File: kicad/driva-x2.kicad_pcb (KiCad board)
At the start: 4 copper layers, 100 x 50 mm, 199 parts, among them J1 CONN_HALL_1, J10 CONN_SPI_2, J11 CONN_CAN, J12 CONN_POWER, J2 CONN_PROG, J3 CONN_USB_OTG, J4 CONN_I2C, J5 CONN_POWER2, J6 CONN_SERVO, J8 CONN_SPI_1, J9 CONN_HALL_2, Q1 TPH1R403NL, Q10 TPH1R403NL, Q11 TPH1R403NL, Q12 TPH1R403NL, Q2 TPH1R403NL, Q3 TPH1R403NL, Q4 TPH1R403NL, Q5 TPH1R403NL, Q6 TPH1R403NL, Q7 TPH1R403NL, Q8 TPH1R403NL, Q9 TPH1R403NL, SW1 push, SW2 push, SW3 push, U1 INA240A2PW, U10 L6387ED, U11 INA240A2PW, U12 L6387ED, U13 AMS1117-3.3, U14 TJA1051T-3, U15 STM32F405RGTx, U2 L6387ED, U3 INA240A2PW, U4 L6387ED, U5 INA240A2PW, U6 L6387ED, U7 INA240A2PW, U8 L6387ED, U9 INA240A2PW

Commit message: Adding 0.9 version
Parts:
- removed C62, C64, C66, C68: 100n, Capacitor_SMD:C_0402_1005Metric
- removed C63, C65, C67: 1n, Capacitor_SMD:C_0402_1005Metric
- removed D10: BLUE, LED_SMD:LED_0603_1608Metric
- removed D11, D6, D7: b5819w, Diode_SMD:D_SOD-123
- removed D8: RED, LED_SMD:LED_0603_1608Metric
- removed D9: GREEN, LED_SMD:LED_0603_1608Metric
- removed H10: PAD_W_2, Connector_Wire:SolderWire-2.5sqmm_1x01_D2.4mm_OD4.4mm
- removed H5: PAD_U_1, Connector_Wire:SolderWire-2.5sqmm_1x01_D2.4mm_OD4.4mm
- removed H6: PAD_V_1, Connector_Wire:SolderWire-2.5sqmm_1x01_D2.4mm_OD4.4mm
- removed H7: PAD_W_1, Connector_Wire:SolderWire-2.5sqmm_1x01_D2.4mm_OD4.4mm
- removed H8: PAD_U_2, Connector_Wire:SolderWire-2.5sqmm_1x01_D2.4mm_OD4.4mm
- removed H9: PAD_V_2, Connector_Wire:SolderWire-2.5sqmm_1x01_D2.4mm_OD4.4mm
- removed Q1, Q10, Q11, Q12, Q2, Q3, Q4, Q5, Q6, Q7, Q8, Q9: TPH1R403NL, Package_SO:SOP-8-1EP_4.57x4.57mm_P1.27mm_EP4.57x4.45mm_ThermalVias
- removed R53: 3K3, Resistor_SMD:R_0402_1005Metric
- removed R54: 4k7, Resistor_SMD:R_0402_1005Metric
- removed R55: 10k, Resistor_SMD:R_0402_1005Metric
- removed R56, R57, R58, R59, R60, R61, R62, R63, R64: 1K, Resistor_SMD:R_0402_1005Metric
- removed TH1, TH2: Thermistor, Resistor_SMD:R_0603_1608Metric
- removed U11: INA240A2PW, Package_SO:TSSOP-8_4.4x3mm_P0.65mm
- removed U12: L6387ED, Package_SO:SOIC-8_3.9x4.9mm_P1.27mm
- removed U13: AMS1117-3.3, Package_TO_SOT_SMD:SOT-223-3_TabPin2
- removed U14: TJA1051T-3, Package_SO:SOIC-8_3.9x4.9mm_P1.27mm
- removed U15: STM32F405RGTx, Package_QFP:LQFP-64_10x10mm_P0.5mm
- added J7: CONN_SPI_1, Connector_PinHeader_2.54mm:PinHeader_1x06_P2.54mm_Vertical, F.Cu at (64.3, 68.8)
- added L1: 2.2uh, Inductor_SMD:L_1210_3225Metric, F.Cu at (110.0, 57.5)
- C1: value 1u -> 10u
- C10, C20, C25, C30, C5, C53: value 10n -> 100n
- C11, C6: value 1u -> 100n; footprint Capacitor_SMD:C_0603_1608Metric -> Capacitor_SMD:C_0402_1005Metric
- C12: value 100p -> 10u
- C13: value 100p -> 4.7u+; footprint Capacitor_SMD:C_0402_1005Metric -> Capacitor_SMD:C_0805_2012Metric
- C14, C4, C9: value 470n -> 100n; footprint Capacitor_SMD:C_0603_1608Metric -> Capacitor_SMD:C_0402_1005Metric
- C16: value 1u -> 12p; footprint Capacitor_SMD:C_0603_1608Metric -> Capacitor_SMD:C_0402_1005Metric
- C17: value 100p -> 12p
- C18, C2, C3, C7, C8: value 100p -> 100n
- C19: value 470n -> 2.2u
- C21: value 1u -> 2.2u
- C22, C23: value 100p -> 2.2u; footprint Capacitor_SMD:C_0402_1005Metric -> Capacitor_SMD:C_0603_1608Metric
- C24: value 470n -> 10u
- C26: value 1u -> 220n+
- C27: value 100p -> 100n+; footprint Capacitor_SMD:C_0402_1005Metric -> Capacitor_SMD:C_0603_1608Metric
- C28: value 100p -> 220n+; footprint Capacitor_SMD:C_0402_1005Metric -> Capacitor_SMD:C_0603_1608Metric
- C29: value 470n -> 1n; footprint Capacitor_SMD:C_0603_1608Metric -> Capacitor_SMD:C_0402_1005Metric
- C31, C54: value 10u -> 220n+
- C32, C37: value 100n -> 100n+; footprint Capacitor_SMD:C_0402_1005Metric -> Capacitor_SMD:C_0603_1608Metric
- C33, C36, C38, C49, C56: value 100n -> 220n+; footprint Capacitor_SMD:C_0402_1005Metric -> Capacitor_SMD:C_0603_1608Metric
- C34, C39: value 100n -> 1n
- C41, C42: value 10u -> 100n; footprint Capacitor_SMD:C_0805_2012Metric -> Capacitor_SMD:C_0402_1005Metric
- C43: value 100n -> 2.2n
- C44: value 10n -> 220n+; footprint Capacitor_SMD:C_0402_1005Metric -> Capacitor_SMD:C_0603_1608Metric
- C45: value 12p -> 100n+; footprint Capacitor_SMD:C_0402_1005Metric -> Capacitor_SMD:C_0603_1608Metric
- C46: value 12p -> 220n+; footprint Capacitor_SMD:C_0402_1005Metric -> Capacitor_SMD:C_0603_1608Metric
- C47, C52: value 2.2u -> 1n; footprint Capacitor_SMD:C_0603_1608Metric -> Capacitor_SMD:C_0402_1005Metric
- C50: value 2.2u -> 100n+
- C51: value 2.2u -> 220n+
- C55: value 10n -> 100n+; footprint Capacitor_SMD:C_0402_1005Metric -> Capacitor_SMD:C_0603_1608Metric
- C59: value 1n -> 33p
- C60: value 100n -> 1000u+; footprint Capacitor_SMD:C_0402_1005Metric -> Capacitor_THT:CP_Radial_D8.0mm_P5.00mm
- C61: value 1n -> 10n
- D2: value b5819w -> RED; footprint Diode_SMD:D_SOD-123 -> LED_SMD:LED_0603_1608Metric
- D3: value b5819w -> GREEN; footprint Diode_SMD:D_SOD-123 -> LED_SMD:LED_0603_1608Metric
- D4: value b5819w -> BLUE; footprint Diode_SMD:D_SOD-123 -> LED_SMD:LED_0603_1608Metric
- H1, H2, H3, H4: footprint MountingHole:MountingHole_3.2mm_M3_Pad_Via -> MountingHole:MountingHole_3.2mm_M3_ISO14580_Pad_TopBottom
- J10: value CONN_SPI_2 -> CONN_CAN; footprint Connector_PinHeader_2.54mm:PinHeader_1x06_P2.54mm_Vertical -> Connector_PinHeader_2.54mm:PinHeader_1x04_P2.54mm_Vertical
- J11: value CONN_CAN -> CONN_PWR; footprint Connector_PinHeader_2.54mm:PinHeader_1x04_P2.54mm_Vertical -> TerminalBlock:TerminalBlock_Altech_AK300-2_P5.00mm
- J12: value CONN_POWER -> CONN_SERIAL; footprint Connector_AMASS:AMASS_XT60-M_1x02_P7.20mm_Vertical -> Connector_PinHeader_2.54mm:PinHeader_1x04_P2.54mm_Vertical
- J2: footprint Connector_PinHeader_2.54mm:PinHeader_1x05_P2.54mm_Vertical -> Connector_PinHeader_2.54mm:PinHeader_1x04_P2.54mm_Vertical
- J3: footprint Connector_USB:USB_Micro-B_GCT_USB3076-30-A -> Connector_USB:USB_Micro-B_Wuerth_629105150521
- J4: value CONN_I2C -> CONN_MOT_1; footprint Connector_PinHeader_2.54mm:PinHeader_1x04_P2.54mm_Vertical -> TerminalBlock:TerminalBlock_Altech_AK300-3_P5.00mm
- J5: value CONN_POWER2 -> CONN_SERIAL; footprint Connector_PinHeader_2.54mm:PinHeader_1x02_P2.54mm_Vertical -> Connector_PinHeader_2.54mm:PinHeader_1x04_P2.54mm_Vertical
- J6: value CONN_SERVO -> CONN_MOT_2; footprint Connector_PinHeader_2.54mm:PinHeader_1x05_P2.54mm_Vertical -> TerminalBlock:TerminalBlock_Altech_AK300-3_P5.00mm
- J8: value CONN_SPI_1 -> CONN_SPI_2
- R10: value 33 -> 220; footprint Resistor_SMD:R_0603_1608Metric -> Resistor_SMD:R_0402_1005Metric
- R11: value 10k -> 2K2; footprint Resistor_SMD:R_0402_1005Metric -> Resistor_SMD:R_0603_1608Metric
- R12, R30, R42: value 0.002R @1W -> 10k; footprint Resistor_SMD:R_1206_3216Metric -> Resistor_SMD:R_0402_1005Metric
- R13, R22, R25, R34, R37: value 33 -> 10k; footprint Resistor_SMD:R_0603_1608Metric -> Resistor_SMD:R_0402_1005Metric
- R14: value 1 -> 120R+; footprint Resistor_SMD:R_0603_1608Metric -> Resistor_SMD:R_1206_3216Metric
- R15: value 10k -> 33K
- R16: value 33 -> 3K3; footprint Resistor_SMD:R_0603_1608Metric -> Resistor_SMD:R_0402_1005Metric
- R18: value 0.002R @1W -> 1K; footprint Resistor_SMD:R_1206_3216Metric -> Resistor_SMD:R_0402_1005Metric
- R19: value 33 -> 1K; footprint Resistor_SMD:R_0603_1608Metric -> Resistor_SMD:R_0402_1005Metric
- R20: value 1 -> 1K; footprint Resistor_SMD:R_0603_1608Metric -> Resistor_SMD:R_0402_1005Metric
- R23, R27, R35, R39: value 10k -> 1k
- R24, R36: value 0.002R @1W -> 510R; footprint Resistor_SMD:R_1206_3216Metric -> Resistor_SMD:R_0402_1005Metric
- R26, R38: value 1 -> 10k; footprint Resistor_SMD:R_0603_1608Metric -> Resistor_SMD:R_0402_1005Metric
- R28, R40: value 33 -> 510R; footprint Resistor_SMD:R_0603_1608Metric -> Resistor_SMD:R_0402_1005Metric
- R31, R43: value 33 -> 1k; footprint Resistor_SMD:R_0603_1608Metric -> Resistor_SMD:R_0402_1005Metric
- R32, R44: value 1 -> 510R; footprint Resistor_SMD:R_0603_1608Metric -> Resistor_SMD:R_0402_1005Metric
- R45: value 10k -> 400K
- R46: value 220 -> 4.7k
- R47: value 2K2 -> 4.7k; footprint Resistor_SMD:R_0603_1608Metric -> Resistor_SMD:R_0402_1005Metric
- R48: value 10k -> 4.7k
- R49: value 10k -> 120k
- R50: value 220 -> 39k
- R51: value 33K -> 10k
- R52: value 4k7 -> 10k
- U1: value INA240A2PW -> mp2451dt; footprint Package_SO:TSSOP-8_4.4x3mm_P0.65mm -> Package_TO_SOT_SMD:SOT-23-6
- U10, U4, U6, U8: value L6387ED -> IFX007T; footprint Package_SO:SOIC-8_3.9x4.9mm_P1.27mm -> Package_TO_SOT_SMD:TO-263-7_TabPin8
- U2: value L6387ED -> TJA1051T-3
- U3: value INA240A2PW -> STM32F405RGTx; footprint Package_SO:TSSOP-8_4.4x3mm_P0.65mm -> Package_QFP:LQFP-64_10x10mm_P0.5mm
- U5, U9: value INA240A2PW -> IFX007T; footprint Package_SO:TSSOP-8_4.4x3mm_P0.65mm -> Package_TO_SOT_SMD:TO-263-7_TabPin8
- U7: value INA240A2PW -> MPU-6050; footprint Package_SO:TSSOP-8_4.4x3mm_P0.65mm -> Sensor_Motion:InvenSense_QFN-24_4x4mm_P0.5mm
- moved H1 102.6 mm to (65.6, 33.6)
- moved R14 101.6 mm to (74.5, 84.8), turned to 0 degrees
- moved H3 98.0 mm to (158.4, 86.5)
- moved J10 85.3 mm to (70.7, 87.8), turned to 90 degrees
- moved U2 84.6 mm to (74.7, 80.0), turned to 270 degrees
- moved U7 82.4 mm to (149.3, 80.3), turned to 90 degrees
- moved R13 79.2 mm to (91.5, 85.5)
- moved C58 77.8 mm to (92.5, 63.9)
- moved C57 77.6 mm to (92.5, 60.9), turned to 0 degrees
- moved R11 77.2 mm to (97.7, 87.8)
- moved C5 77.1 mm to (102.4, 81.0)
- moved R17 72.0 mm to (80.8, 85.0), turned to 90 degrees
- moved J4 71.0 mm to (66.4, 50.3)
- moved J6 70.1 mm to (157.6, 50.2)
- moved R18 62.6 mm to (101.3, 87.3), turned to 90 degrees
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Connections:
- C1 pad 1: Net-(C1-Pad1) -> GND
- C1 pad 2: Net-(C1-Pad2) -> +3V3
- C10 pad 1: Net-(C10-Pad1) -> GND
- C10 pad 2: GND -> +3V3
- C12 pad 1: /driver_2/HIN_W -> GND
- C12 pad 2: GND -> +3V3
- C13 pad 1: /driver_2/LIN_W -> GND
- C13 pad 2: GND -> Net-(C13-Pad2)
- C14 pad 1: VCC -> GND
- C14 pad 2: GND -> +3.3VA
- C15 pad 1: Net-(C15-Pad1) -> GND
- C15 pad 2: GND -> +3.3VA
- C16 pad 1: Net-(C16-Pad1) -> HSE_IN
- C16 pad 2: Net-(C16-Pad2) -> GND
- C17 pad 1: /driver_1/HIN_U -> Net-(C17-Pad1)
- C18 pad 1: /driver_1/LIN_U -> BOOT0
- C19 pad 1: VCC -> GND
- C19 pad 2: GND -> +3V3
- C2 pad 1: /driver_2/HIN_U -> GND
- C2 pad 2: GND -> +3V3
- C20 pad 1: Net-(C20-Pad1) -> NRST
- C21 pad 1: Net-(C21-Pad1) -> GND
- C21 pad 2: Net-(C21-Pad2) -> +3V3
- C22 pad 1: /driver_1/HIN_V -> Net-(C22-Pad1)
- C23 pad 1: /driver_1/LIN_V -> Net-(C23-Pad1)
- C24 pad 1: VCC -> GND
- C24 pad 2: GND -> BATTERY
- C25 pad 1: Net-(C25-Pad1) -> USER_BUTTON
- C26 pad 1: Net-(C26-Pad1) -> /driver-2/OUT_U
- C26 pad 2: Net-(C26-Pad2) -> VCC
- C27 pad 1: /driver_1/HIN_W -> VCC
- C28 pad 1: /driver_1/LIN_W -> VCC
- C29 pad 1: VCC -> /driver-2/SENSE_U
- C3 pad 1: /driver_2/LIN_U -> GND
- C3 pad 2: GND -> +3V3
- C31 pad 1: GND -> /driver-2/OUT_V
- C31 pad 2: +3V3 -> VCC
- C32 pad 1: GND -> VCC
- C32 pad 2: +3V3 -> GND
- C33 pad 1: GND -> VCC
- C33 pad 2: +3V3 -> GND
- C34 pad 1: GND -> /driver-2/SENSE_V
- C34 pad 2: +3V3 -> GND
- C35 pad 1: GND -> Net-(C35-Pad1)
- C35 pad 2: +3V3 -> GND
- C36 pad 1: GND -> /driver-2/OUT_W
- C36 pad 2: +3V3 -> VCC
- C37 pad 1: GND -> VCC
- C37 pad 2: +3V3 -> GND
- C38 pad 1: GND -> VCC
- C38 pad 2: +3V3 -> GND
- C39 pad 1: GND -> /driver-2/SENSE_W
- C39 pad 2: +3V3 -> GND
- C4 pad 1: VCC -> GND
- C4 pad 2: GND -> +3V3
- C40 pad 1: GND -> Net-(C40-Pad1)
- C40 pad 2: +3V3 -> GND
- C41 pad 2: Net-(C41-Pad2) -> +3V3
- C42 pad 2: +3V3 -> Net-(C42-Pad2)
- C43 pad 2: +3.3VA -> Net-(C43-Pad2)
- C44 pad 1: GND -> /driver-1/OUT_U
- C44 pad 2: +3.3VA -> VCC
- C45 pad 1: HSE_IN -> VCC
- C46 pad 1: Net-(C46-Pad1) -> VCC
- C47 pad 1: GND -> /driver-1/SENSE_U
- C47 pad 2: +3V3 -> GND
- C48 pad 1: BOOT0 -> Net-(C48-Pad1)
- C49 pad 1: NRST -> /driver-1/OUT_V
- C49 pad 2: GND -> VCC
- C5 pad 1: Net-(C5-Pad1) -> GND
- C5 pad 2: GND -> +3V3
- C50 pad 1: GND -> VCC
- C50 pad 2: +3V3 -> GND
- C51 pad 1: Net-(C51-Pad1) -> VCC
- C52 pad 1: Net-(C52-Pad1) -> /driver-1/SENSE_V
- C53 pad 1: TEMP_1 -> Net-(C53-Pad1)
- C54 pad 1: GND -> /driver-1/OUT_W
- C54 pad 2: BATTERY -> VCC
- C55 pad 1: TEMP_2 -> VCC
- C56 pad 1: USER_BUTTON -> VCC
- C57 pad 1: /driver_2/SENSE_U -> /driver-1/SENSE_W
- C58 pad 1: +3V3 -> Net-(C58-Pad1)
- C59 pad 1: /driver_2/SENSE_V -> Net-(C59-Pad1)
- C59 pad 2: GND -> +3V3
- C6 pad 1: Net-(C6-Pad1) -> GND
- C6 pad 2: Net-(C6-Pad2) -> +3V3
- C60 pad 1: +3V3 -> VCC
- C61 pad 1: /driver_2/SENSE_W -> +3V3
- C7 pad 1: /mcu/HIN_U_2 -> GND
- C7 pad 2: GND -> +3V3
- C8 pad 1: /mcu/LIN_U_2 -> GND
- C8 pad 2: GND -> +3V3
- C9 pad 1: VCC -> GND
- C9 pad 2: GND -> +3V3
- D1 pad 1: Net-(C1-Pad2) -> Net-(D1-Pad1)
- D2 pad 1: Net-(C6-Pad2) -> Net-(D2-Pad1)
- D2 pad 2: VCC -> +3V3
- D3 pad 1: Net-(C11-Pad2) -> Net-(D3-Pad1)
- D3 pad 2: VCC -> LED_GREEN
- D4 pad 1: Net-(C16-Pad2) -> Net-(D4-Pad1)
- D4 pad 2: VCC -> LED_BLUE
- D5 pad 1: Net-(C21-Pad2) -> Net-(C11-Pad1)
- D5 pad 2: VCC -> GND
- FB1 pad 1: Net-(C41-Pad2) -> Net-(C13-Pad2)
- FB1 pad 2: Net-(D11-Pad1) -> Net-(D1-Pad1)
- HSE1 pad 3: Net-(C46-Pad1) -> Net-(C17-Pad1)
- J1 pad 2: /mcu/HALL_U_1 -> /mcu/HALL_U1
- J1 pad 3: /mcu/HALL_V_1 -> /mcu/HALL_V1
- J1 pad 4: /mcu/HALL_W_1 -> /mcu/HALL_W1
- J10 pad 2: /mcu/SPI3_SS2 -> /mcu/CAN_L
- J10 pad 3: /mcu/SPI3_MISO -> /mcu/CAN_H
- J10 pad 4: /mcu/SPI3_MOSI -> +3V3
- J11 pad 2: /mcu/CAN_H -> VCC
- J12 pad 2: VCC -> /mcu/I2C1_SCL
- J2 pad 1: /mcu/JTAG_DO -> /mcu/SWO
- J2 pad 2: /mcu/JTAG_DI -> /mcu/SWCLK
- J2 pad 3: /mcu/SWCLK -> GND
- J2 pad 4: GND -> /mcu/SWDIO
- J4 pad 1: GND -> /driver-1/OUT_W
- J4 pad 2: /mcu/I2C_1_SCL -> /driver-1/OUT_V
- J4 pad 3: /mcu/I2C_1_SDA -> /driver-1/OUT_U
- J5 pad 1: Net-(J3-Pad1) -> GND
- J5 pad 2: ALT_POWER -> /mcu/USART1_TX
- J6 pad 1: GND -> /driver-2/OUT_W
- J6 pad 2: /mcu/USART1_TX -> /driver-2/OUT_V
- J6 pad 3: /mcu/USART1_RX -> /driver-2/OUT_U
- J8 pad 2: /mcu/SPI3_SS1 -> /mcu/SPI3_SS2
- J8 pad 3: /mcu/SPI3_MISO -> SPI3_MOSI
- J8 pad 4: /mcu/SPI3_MOSI -> SPI3_MISO
- J8 pad 5: /mcu/SPI3_SCLK -> SPI3_SCLK
- J9 pad 2: /mcu/HALL_U_I2C_2_SCL -> /mcu/HALL_U2
- J9 pad 3: /mcu/HALL_V_I2C_2_SDA -> /mcu/HALL_V2
- J9 pad 4: /mcu/HALL_W_2 -> /mcu/HALL_W2
- R10 pad 1: Net-(Q1-Pad4) -> HSE_OUT
- R10 pad 2: Net-(C1-Pad1) -> Net-(C17-Pad1)
- R11 pad 1: Net-(Q1-Pad1) -> NRST
- R11 pad 2: Net-(Q1-Pad4) -> +3V3
- R12 pad 1: /driver_2/OUT_U -> GND
- R12 pad 2: Net-(Q1-Pad1) -> BOOT1
- R13 pad 1: Net-(Q2-Pad4) -> GND
- R13 pad 2: Net-(R13-Pad2) -> BOOT0
- R14 pad 1: Net-(C5-Pad1) -> /mcu/CAN_L
- R14 pad 2: Net-(Q1-Pad1) -> /mcu/CAN_H
- R15 pad 1: GND -> BATTERY
- R15 pad 2: Net-(Q2-Pad4) -> VCC
- R16 pad 1: Net-(Q3-Pad4) -> GND
- R16 pad 2: Net-(C6-Pad1) -> BATTERY
- R17 pad 1: Net-(Q3-Pad1) -> USER_BUTTON
- R17 pad 2: Net-(Q3-Pad4) -> GND
- R18 pad 1: /driver_2/OUT_V -> GND
- R18 pad 2: Net-(Q3-Pad1) -> Net-(D2-Pad1)
- R19 pad 1: Net-(Q4-Pad4) -> GND
- R19 pad 2: Net-(R19-Pad2) -> Net-(D3-Pad1)
- R20 pad 1: Net-(C10-Pad1) -> GND
- R20 pad 2: Net-(Q3-Pad1) -> Net-(D4-Pad1)
- R21 pad 1: GND -> Net-(R21-Pad1)
- R21 pad 2: Net-(Q4-Pad4) -> /driver-2/IN_U
- R22 pad 1: Net-(Q5-Pad4) -> Net-(R22-Pad1)
- R22 pad 2: Net-(C11-Pad1) -> /driver-2/EN_U
- R23 pad 1: Net-(Q5-Pad1) -> /driver-2/SENSE_U
- R23 pad 2: Net-(Q5-Pad4) -> GND
- R24 pad 1: /driver_2/OUT_W -> Net-(C30-Pad1)
- R24 pad 2: Net-(Q5-Pad1) -> GND
- R25 pad 1: Net-(Q6-Pad4) -> Net-(R25-Pad1)
- R25 pad 2: Net-(R25-Pad2) -> /driver-2/IN_V
- R26 pad 1: Net-(C15-Pad1) -> Net-(R26-Pad1)
- R26 pad 2: Net-(Q5-Pad1) -> /driver-2/EN_V
- R27 pad 1: GND -> /driver-2/SENSE_V
- R27 pad 2: Net-(Q6-Pad4) -> GND
- R28 pad 1: Net-(Q7-Pad4) -> Net-(C35-Pad1)
- R28 pad 2: Net-(C16-Pad1) -> GND
- R29 pad 1: Net-(Q7-Pad1) -> Net-(R29-Pad1)
- R29 pad 2: Net-(Q7-Pad4) -> /driver-2/IN_W
- R30 pad 1: /driver_1/OUT_U -> Net-(R30-Pad1)
- R30 pad 2: Net-(Q7-Pad1) -> /driver-2/EN_W
- R31 pad 1: Net-(Q8-Pad4) -> /driver-2/SENSE_W
- R31 pad 2: Net-(R31-Pad2) -> GND
- R32 pad 1: Net-(C20-Pad1) -> Net-(C40-Pad1)
- R32 pad 2: Net-(Q7-Pad1) -> GND
- R33 pad 1: GND -> Net-(R33-Pad1)
- R33 pad 2: Net-(Q8-Pad4) -> /driver-1/IN_U
- R34 pad 1: Net-(Q9-Pad4) -> Net-(R34-Pad1)
- R34 pad 2: Net-(C21-Pad1) -> /driver-1/EN_U
- R35 pad 1: Net-(Q10-Pad5) -> /driver-1/SENSE_U
- R35 pad 2: Net-(Q9-Pad4) -> GND
- R36 pad 1: /driver_1/OUT_V -> Net-(C48-Pad1)
- R36 pad 2: Net-(Q10-Pad5) -> GND
- R37 pad 1: Net-(Q10-Pad4) -> Net-(R37-Pad1)
- R37 pad 2: Net-(R37-Pad2) -> /driver-1/IN_V
- R38 pad 1: Net-(C25-Pad1) -> Net-(R38-Pad1)
- R38 pad 2: Net-(Q10-Pad5) -> /driver-1/EN_V
- R39 pad 1: GND -> /driver-1/SENSE_V
- R39 pad 2: Net-(Q10-Pad4) -> GND
- R4 pad 2: /mcu/HALL_W_1 -> /mcu/HALL_W1
- R40 pad 1: Net-(Q11-Pad4) -> Net-(C53-Pad1)
- R40 pad 2: Net-(C26-Pad1) -> GND
- R41 pad 1: Net-(Q11-Pad1) -> Net-(R41-Pad1)
- R41 pad 2: Net-(Q11-Pad4) -> /driver-1/IN_W
- R42 pad 1: /driver_1/OUT_W -> Net-(R42-Pad1)
- R42 pad 2: Net-(Q11-Pad1) -> /driver-1/EN_W
- R43 pad 1: Net-(Q12-Pad4) -> /driver-1/SENSE_W
- R43 pad 2: Net-(R43-Pad2) -> GND
- R44 pad 1: Net-(C30-Pad1) -> Net-(C58-Pad1)
- R44 pad 2: Net-(Q11-Pad1) -> GND
- R45 pad 1: GND -> Net-(R45-Pad1)
- R45 pad 2: Net-(Q12-Pad4) -> Net-(C13-Pad2)
- R46 pad 1: HSE_OUT -> +3V3
- R46 pad 2: Net-(C46-Pad1) -> /mcu/I2C1_SCL
- R47 pad 1: NRST -> +3V3
- R47 pad 2: +3V3 -> /mcu/I2C1_SDA
- R48 pad 1: GND -> Net-(R48-Pad1)
- R48 pad 2: BOOT1 -> GND
- R49 pad 1: GND -> +3V3
- R49 pad 2: BOOT0 -> Net-(C59-Pad1)
- R5 pad 2: /mcu/HALL_V_1 -> /mcu/HALL_V1
- R50 pad 1: /mcu/CAN_L -> Net-(C59-Pad1)
- R50 pad 2: /mcu/CAN_H -> GND
- R51 pad 1: BATTERY -> Net-(R51-Pad1)
- R51 pad 2: VCC -> GND
- R52 pad 1: GND -> Net-(R52-Pad1)
- R52 pad 2: TEMP_1 -> GND
- R6 pad 2: /mcu/HALL_U_1 -> /mcu/HALL_U1
- R7 pad 2: /mcu/HALL_W_2 -> /mcu/HALL_W2
- R8 pad 2: /mcu/HALL_V_I2C_2_SDA -> /mcu/HALL_V2
- R9 pad 2: /mcu/HALL_U_I2C_2_SCL -> /mcu/HALL_U2
- U1 pad 1: GND -> Net-(C11-Pad2)
- U1 pad 2: Net-(Q1-Pad1) -> GND
- U1 pad 3: /driver_2/OUT_U -> Net-(C59-Pad1)
- U1 pad 4: GND -> Net-(R45-Pad1)
- U1 pad 5: +3V3 -> Net-(C13-Pad2)
- U1 pad 6: +3V3 -> Net-(C11-Pad1)
- U10 pad 1: /driver_1/LIN_V -> GND
- U10 pad 2: /driver_1/HIN_V -> Net-(R41-Pad1)
- U10 pad 3: VCC -> Net-(R42-Pad1)
- U10 pad 4: GND -> /driver-1/OUT_W
- U10 pad 5: Net-(C21-Pad2) -> Net-(C58-Pad1)
- U10 pad 6: Net-(C21-Pad1) -> /driver-1/SENSE_W
- U10 pad 7: Net-(Q10-Pad5) -> VCC
- U10 pad 8: Net-(R37-Pad2) -> /driver-1/OUT_W
- U2 pad 1: /driver_2/LIN_U -> CAN2_TX
- U2 pad 2: /driver_2/HIN_U -> GND
- U2 pad 3: VCC -> +3V3
- U2 pad 4: GND -> CAN2_RX
- U2 pad 5: Net-(C1-Pad2) -> +3V3
- U2 pad 6: Net-(C1-Pad1) -> /mcu/CAN_L
- U2 pad 7: Net-(Q1-Pad1) -> /mcu/CAN_H
- U2 pad 8: Net-(R13-Pad2) -> GND
- U3 pad 1: GND -> +3V3
- U3 pad 2: Net-(Q3-Pad1) -> /mcu/SPI3_SS1
- U3 pad 3: /driver_2/OUT_V -> /mcu/SPI3_SS2
- U3 pad 4: GND -> Net-(U3-Pad4)
- U3 pad 5: +3V3 -> HSE_IN
- U3 pad 6: +3V3 -> HSE_OUT
- U3 pad 7: GND -> NRST
- U3 pad 8: Net-(R60-Pad2) -> /driver-2/SENSE_U
- U4 pad 1: /mcu/LIN_U_2 -> GND
- U4 pad 2: /mcu/HIN_U_2 -> Net-(R21-Pad1)
- U4 pad 3: VCC -> Net-(R22-Pad1)
- U4 pad 4: GND -> /driver-2/OUT_U
- U4 pad 5: Net-(C6-Pad2) -> Net-(C30-Pad1)
- U4 pad 6: Net-(C6-Pad1) -> /driver-2/SENSE_U
- U4 pad 7: Net-(Q3-Pad1) -> VCC
- U4 pad 8: Net-(R19-Pad2) -> /driver-2/OUT_U
- U5 pad 2: Net-(Q5-Pad1) -> Net-(R25-Pad1)
- U5 pad 3: /driver_2/OUT_W -> Net-(R26-Pad1)
- U5 pad 4: GND -> /driver-2/OUT_V
- U5 pad 5: +3V3 -> Net-(C35-Pad1)
- U5 pad 6: +3V3 -> /driver-2/SENSE_V
- U5 pad 7: GND -> VCC
- U5 pad 8: Net-(R61-Pad2) -> /driver-2/OUT_V
- U6 pad 1: /driver_2/LIN_W -> GND
- U6 pad 2: /driver_2/HIN_W -> Net-(R29-Pad1)
- U6 pad 3: VCC -> Net-(R30-Pad1)
- U6 pad 4: GND -> /driver-2/OUT_W
- U6 pad 5: Net-(C11-Pad2) -> Net-(C40-Pad1)
- U6 pad 6: Net-(C11-Pad1) -> /driver-2/SENSE_W
- U6 pad 7: Net-(Q5-Pad1) -> VCC
- U6 pad 8: Net-(R25-Pad2) -> /driver-2/OUT_W
- U7 pad 1: GND -> Net-(R52-Pad1)
- U7 pad 2: Net-(Q7-Pad1) -> (no net)
- U7 pad 3: /driver_1/OUT_U -> (no net)
- U7 pad 4: GND -> (no net)
- U7 pad 5: +3V3 -> (no net)
- U7 pad 6: +3V3 -> Net-(U7-Pad6)
- U7 pad 7: GND -> Net-(U7-Pad7)
- U7 pad 8: Net-(R62-Pad2) -> +3V3
- U8 pad 1: /driver_1/LIN_U -> GND
- U8 pad 2: /driver_1/HIN_U -> Net-(R33-Pad1)
- U8 pad 3: VCC -> Net-(R34-Pad1)
- U8 pad 4: GND -> /driver-1/OUT_U
- U8 pad 5: Net-(C16-Pad2) -> Net-(C48-Pad1)
- U8 pad 6: Net-(C16-Pad1) -> /driver-1/SENSE_U
- U8 pad 7: Net-(Q7-Pad1) -> VCC
- U8 pad 8: Net-(R31-Pad2) -> /driver-1/OUT_U
- U9 pad 2: Net-(Q10-Pad5) -> Net-(R37-Pad1)
- U9 pad 3: /driver_1/OUT_V -> Net-(R38-Pad1)
- U9 pad 4: GND -> /driver-1/OUT_V
- U9 pad 5: +3V3 -> Net-(C53-Pad1)
- U9 pad 6: +3V3 -> /driver-1/SENSE_V
- U9 pad 7: GND -> VCC
- U9 pad 8: Net-(R63-Pad2) -> /driver-1/OUT_V
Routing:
- net SPI3_MOSI: track 0.00 -> 120.6 mm, vias 0 -> 2
- net SPI3_MISO: track 0.00 -> 116.2 mm, vias 0 -> 3
- net SPI3_SCLK: track 0.00 -> 111.8 mm, vias 0 -> 2
- net Net-(D11-Pad1): track 110.4 -> 0.00 mm, vias 7 -> 0
- net /mcu/SPI3_SCLK: track 103.4 -> 0.00 mm, vias 5 -> 0
- net /mcu/SPI3_MOSI: track 101.4 -> 0.00 mm, vias 5 -> 0
- net /mcu/SPI3_MISO: track 101.3 -> 0.00 mm, vias 5 -> 0
- net /driver_2/SENSE_U: track 81.6 -> 0.00 mm, vias 4 -> 0
- net /mcu/HALL_V2: track 0.00 -> 75.4 mm, vias 0 -> 2
- net /driver_1/LIN_W: track 75.2 -> 0.00 mm, vias 4 -> 0
- net /mcu/HALL_U2: track 0.00 -> 71.7 mm, vias 0 -> 2
- net /mcu/HALL_U1: track 0.00 -> 69.6 mm, vias 0 -> 2
- net /mcu/HALL_W2: track 0.00 -> 69.0 mm, vias 0 -> 2
- net /driver_1/SENSE_W: track 67.7 -> 0.00 mm, vias 3 -> 0
- net /mcu/HALL_V1: track 0.00 -> 67.2 mm, vias 0 -> 2
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- added copper zone on B.Cu, net +3V3
- added copper zone on In2.Cu, net GND
- removed copper zone on In2.Cu, net +3V3
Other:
- board size 100 x 50 mm -> 100 x 67 mm
- board text added: "+"
- board text added: "-"
- board text added: "BOOT"
- board text added: "HALL1"
- board text added: "HALL2"
- board text added: "HALL_U1"
- board text added: "HALL_U2"
- board text added: "HALL_V1"
- board text added: "HALL_V2"
- board text added: "HALL_W1"
- board text added: "HALL_W2"
- board text added: "MOT1"
- board text added: "MOT2"
- board text added: "POWER"
- board text added: "RESET"
- board text added: "SPI1"
- board text added: "SPI3"
- board text added: "SWO"
- board text added: "SimpleFOC Driva Duo v0.9"
- board text added: "U"
- board text added: "USART"
- board text added: "USER"
- board text added: "V"
- board text added: "VCC"
- board text added: "W"
- board text removed: "DANGER !"
- board text removed: "DRIVA x2 v0.5 ALPHA"
- board text removed: "HALL 1"
- board text removed: "HALL 2"
- board text removed: "HALL_U_1"
- board text removed: "HALL_V_1"
- board text removed: "HALL_W_1"
- board text removed: "HALL_W_2"
- board text removed: "JLCJLCJLCJLC"
- board text removed: "JTAG_DI"
- board text removed: "JTAG_DO"
- board text removed: "SCL_HALL_U_2"
- board text removed: "SDA_HALL_V_2"
- board text removed: "SERVO"
- board text removed: "SPI 1"
- board text removed: "SPI 2"
- board text removed: "U1"
- board text removed: "U2"
- board text removed: "USART/PWM"
- board text removed: "USB OTG"
- board text removed: "V1"
- board text removed: "V2"
- board text removed: "VBUS"
- board text removed: "VBUS 5V"
- board text removed: "W1"
- board text removed: "W2"
- board text removed: "github.com/owennewo"

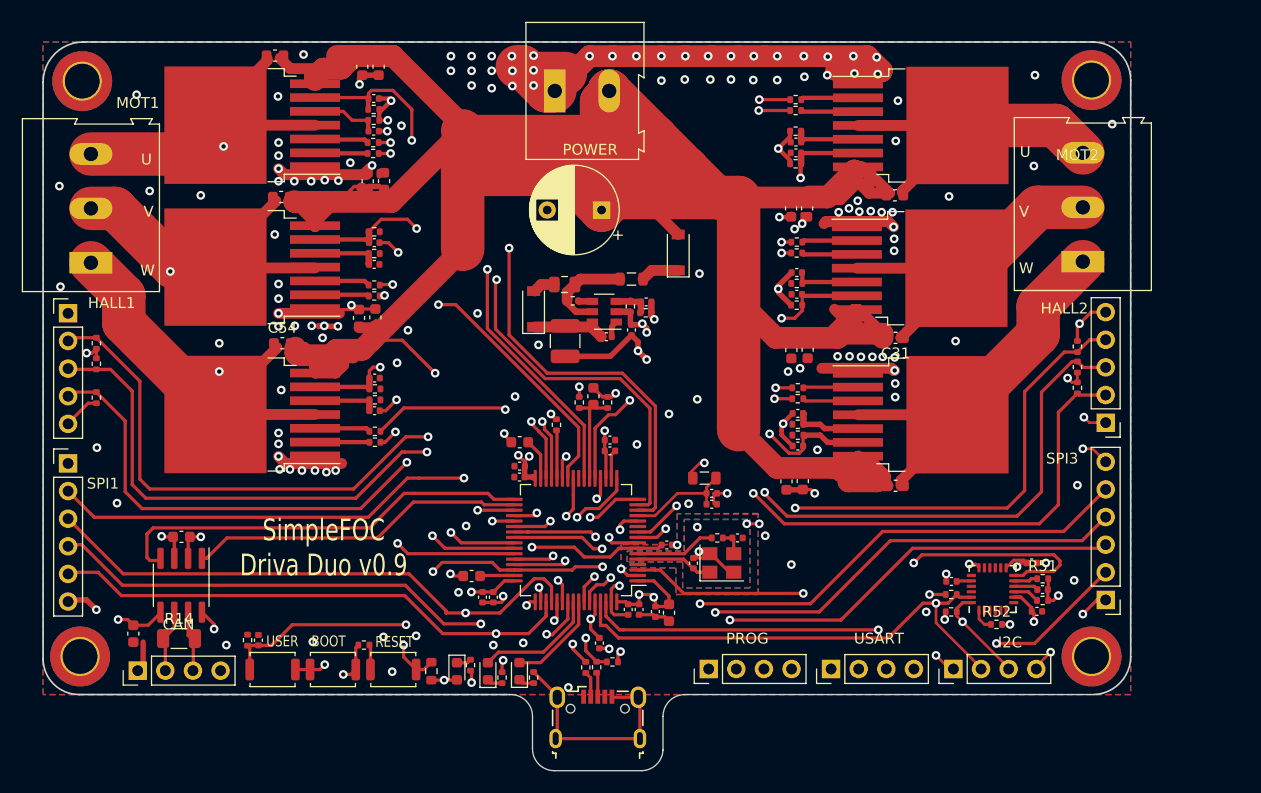
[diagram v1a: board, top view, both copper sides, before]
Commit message: adding solder bridge and more vias under driver
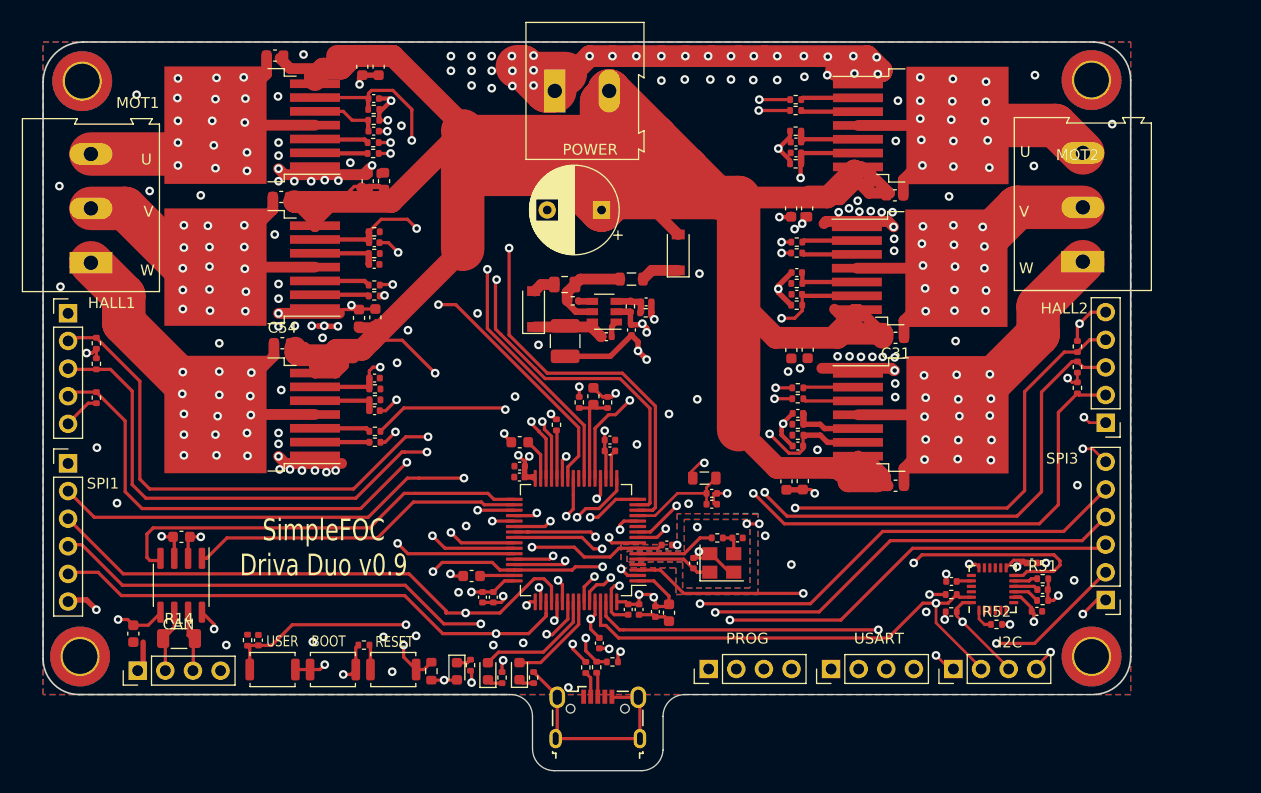
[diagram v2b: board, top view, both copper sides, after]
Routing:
- net /driver-1/OUT_U: track 30.5 -> 30.0 mm, vias 1 -> 15
- net /driver-1/OUT_W: track 36.3 -> 36.6 mm, vias 1 -> 15
- net /driver-1/OUT_V: track 32.2 -> 32.4 mm, vias 1 -> 15
- net /driver-2/OUT_U: track 30.0 -> 30.2 mm, vias 0 -> 15
- net /driver-2/OUT_V: track 31.6 -> 31.5 mm, vias 0 -> 15
- net /driver-2/OUT_W: track 36.7 -> 36.6 mm, vias 0 -> 15

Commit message: updating bom and pos files
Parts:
- added JP1: LDO Solder Bridge, Jumper:SolderJumper-2_P1.3mm_Bridged_Pad1.0x1.5mm, F.Cu at (117.8, 58.0)
- R18, R19, R20: value 1K -> 1k
- R45: value 400K -> 300K
- moved C12 0.10 mm to (116.0, 56.5)
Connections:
- C12 pad 2: +3V3 -> Net-(C12-Pad2)
- C59 pad 2: +3V3 -> Net-(C12-Pad2)
- L1 pad 2: +3V3 -> Net-(C12-Pad2)
- R49 pad 1: +3V3 -> Net-(C12-Pad2)
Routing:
- net Net-(C12-Pad2): track 0.00 -> 13.0 mm
- net +3V3: track 95.9 -> 86.8 mm, vias 26 -> 25

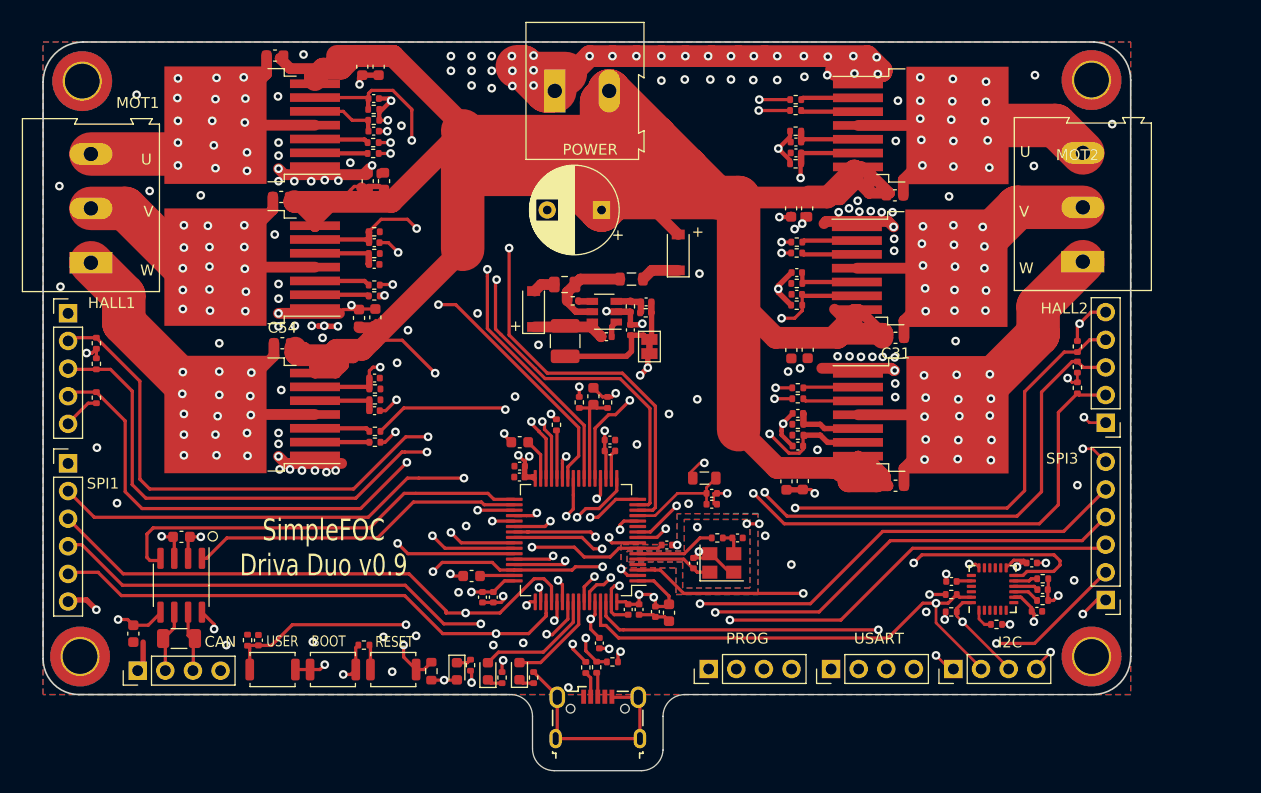
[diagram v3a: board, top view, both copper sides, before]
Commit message: v0.9.1 swapping can to 3.3v SN65HVD230
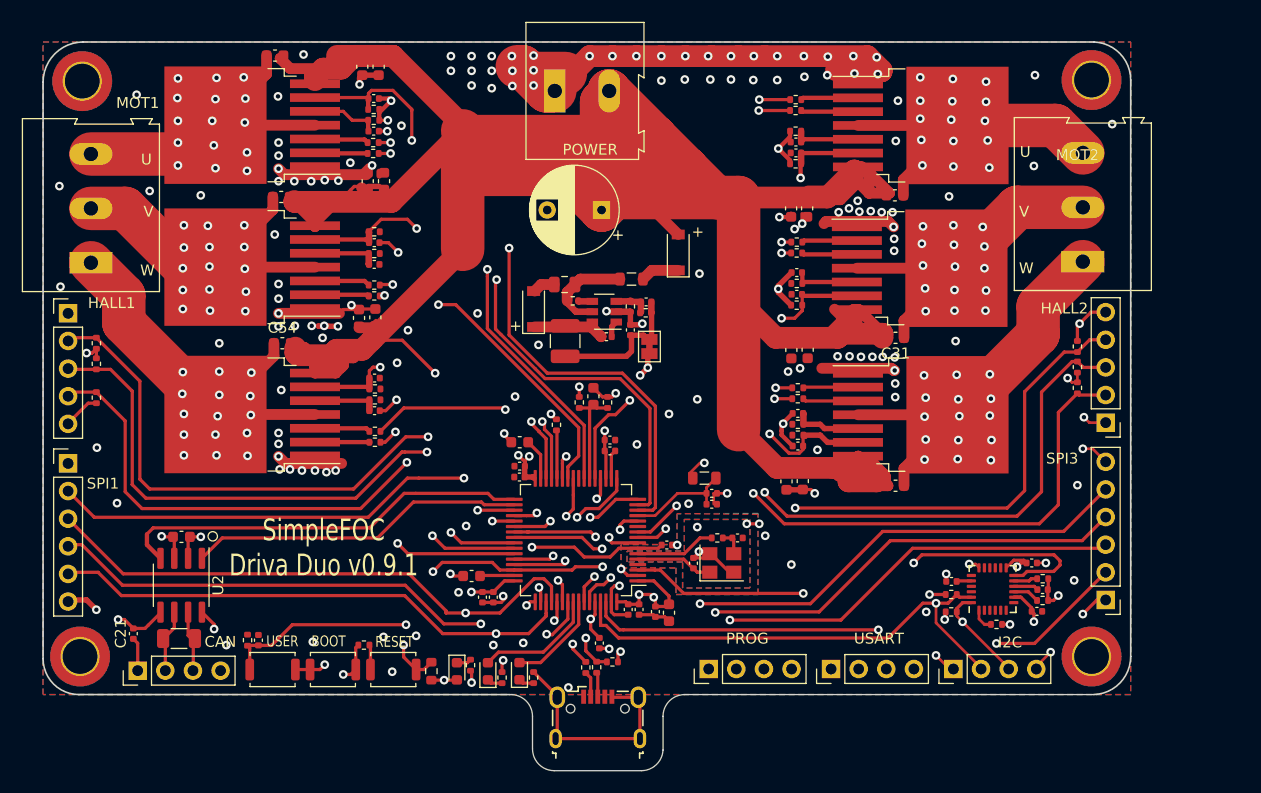
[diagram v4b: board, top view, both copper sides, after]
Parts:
- C21: value 2.2u -> 100n; footprint Capacitor_SMD:C_0603_1608Metric -> Capacitor_SMD:C_0402_1005Metric
- U2: value TJA1051T-3 -> SN65HVD230
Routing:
- net VCC: track 357.8 -> 369.0 mm
- net GND: track 212.4 -> 213.3 mm
- net CAN2_RX: track 39.1 -> 38.3 mm
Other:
- board text added: "SimpleFOC Driva Duo v0.9.1"
- board text removed: "SimpleFOC Driva Duo v0.9"
